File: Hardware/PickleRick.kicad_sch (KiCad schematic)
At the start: 60 parts, among them J1 Conn_01x03_Pin, J2 RBUS, J4 ST1W008S4TR2000, J5 Conn_01x07_Socket, J6 Conn_01x03_Male, U1 ESP32-S3, U2 DPS368, Y1 R940000171

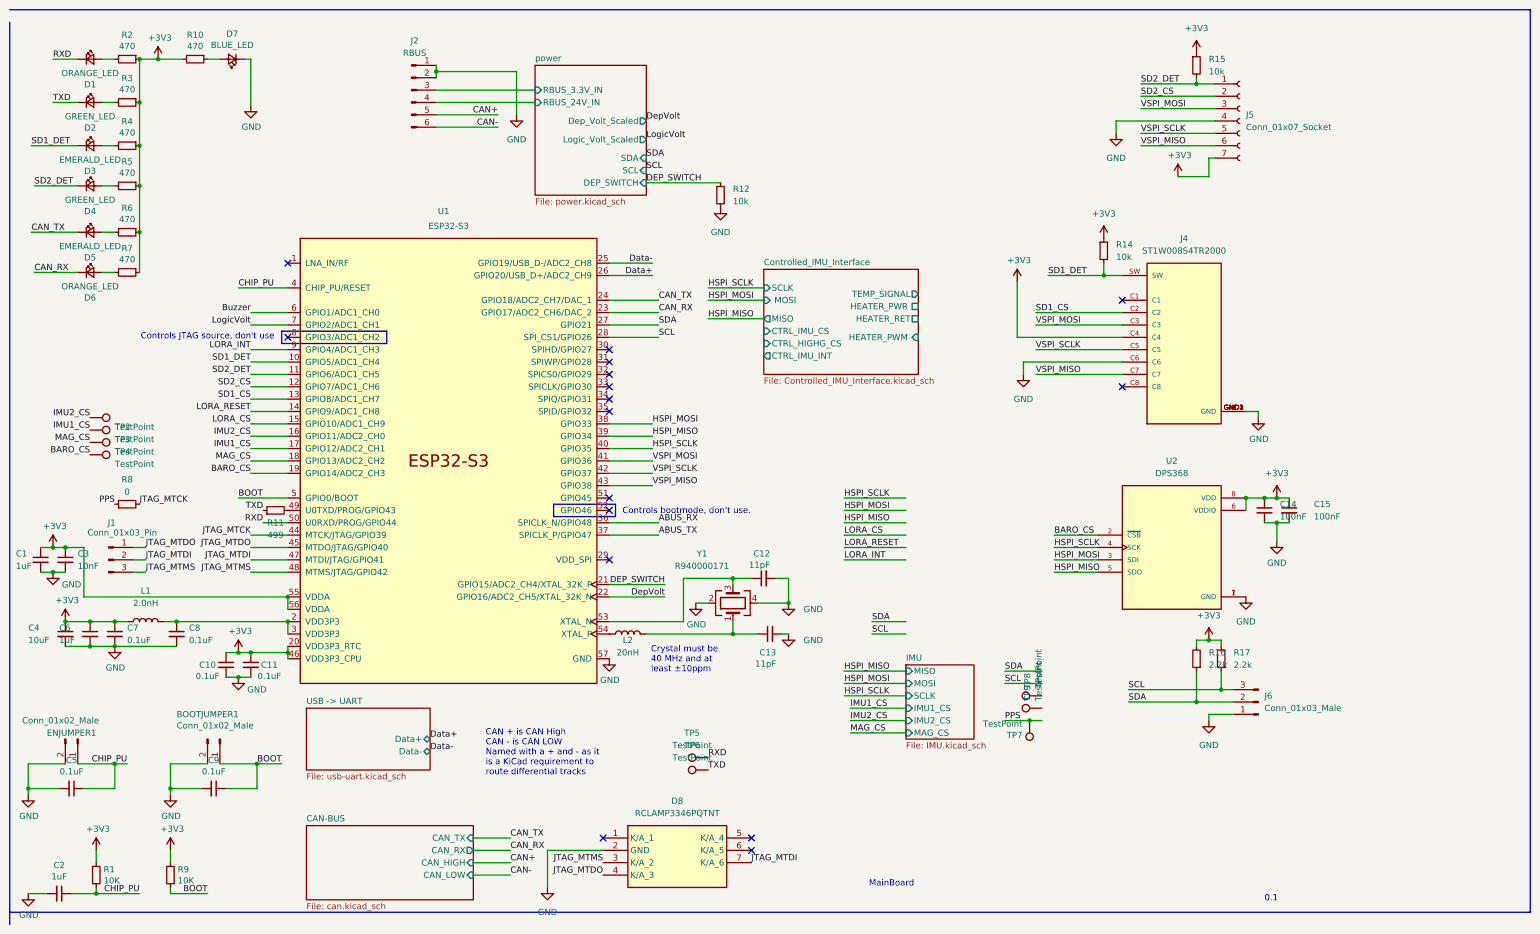
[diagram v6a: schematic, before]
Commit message: Updated Baseboard design but with power supply problems
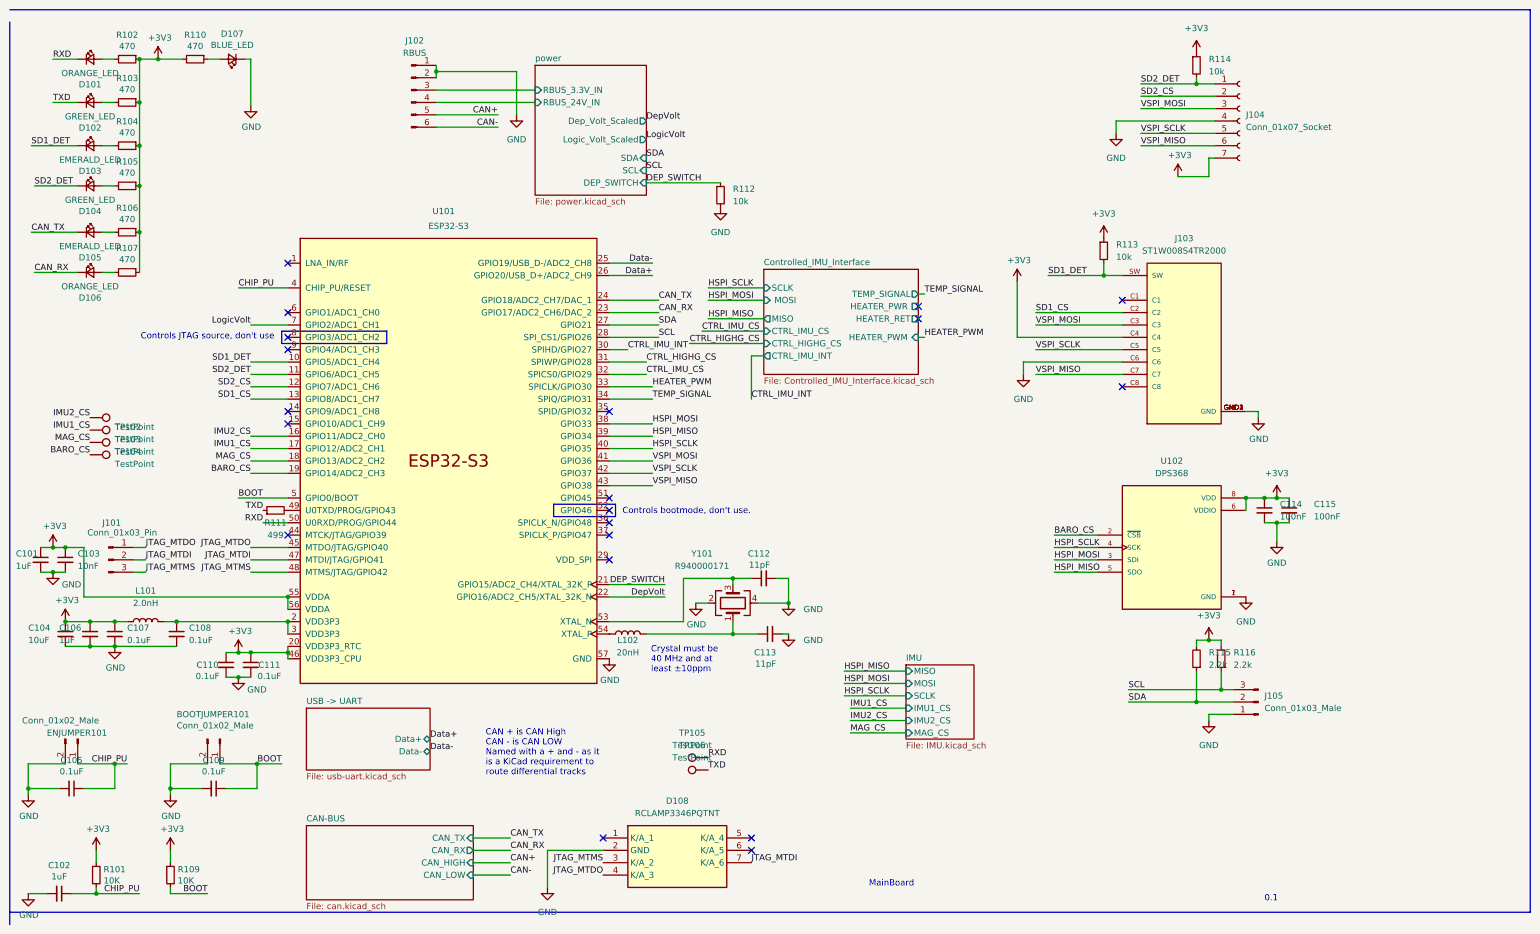
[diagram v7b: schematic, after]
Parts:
- removed R8: 0, Resistor_SMD:R_0402_1005Metric, symbol Device:R_Small
- removed TP7, TP8, TP9: TestPoint, TestPoint:TestPoint_Pad_D1.0mm, symbol Connector:TestPoint
- renumbered BOOTJUMPER1 to BOOTJUMPER101, C1 to C101, C2 to C102, C3 to C103, C4 to C104, C5 to C105, C6 to C106, C7 to C107, C8 to C108, C9 to C109, C10 to C110, C11 to C111, C12 to C112, C13 to C113, C14 to C114, C15 to C115, D1 to D101, D2 to D102, D3 to D103, D4 to D104, D5 to D105, D6 to D106, D7 to D107, D8 to D108, ENJUMPER1 to ENJUMPER101, J1 to J101, J2 to J102, J4 to J103, J5 to J104, J6 to J105, L1 to L101, L2 to L102, R1 to R101, R2 to R102, R3 to R103, R4 to R104, R5 to R105, R6 to R106, R7 to R107, R9 to R109, R10 to R110, R11 to R111, R12 to R112, R14 to R113, R15 to R114, R16 to R115, R17 to R116, TP1 to TP101, TP2 to TP102, TP3 to TP103, TP4 to TP104, TP5 to TP105, TP6 to TP106, U1 to U101, U2 to U102, Y1 to Y101
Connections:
- net CTRL_IMU_INT: now reaches U101.30 (SPIHD/GPIO27)
- net CTRL_HIGHG_CS: now reaches U101.31 (SPIWP/GPIO28)
- net CTRL_IMU_CS: now reaches U101.32 (SPICS0/GPIO29)
- net HEATER_PWM: now reaches U101.33 (SPICLK/GPIO30)
- net TEMP_SIGNAL: now reaches U101.34 (SPIQ/GPIO31)
- net ABUS_RX: no longer names the net of U101.36 (SPICLK_N/GPIO48)
- net ABUS_TX: no longer names the net of U101.37 (SPICLK_P/GPIO47)
- net Buzzer: no longer names the net of U101.6 (GPIO1/ADC1_CH0)
- net JTAG_MTCK: no longer names the net of U101.44 (MTCK/JTAG/GPIO39)
- net LORA_CS: no longer names the net of U101.15 (GPIO10/ADC1_CH9)
- net LORA_INT: no longer names the net of U101.9 (GPIO4/ADC1_CH3)
- net LORA_RESET: no longer names the net of U101.14 (GPIO9/ADC1_CH8)
- no-connect marks 16 -> 20
